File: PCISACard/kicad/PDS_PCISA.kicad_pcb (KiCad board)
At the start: 2 copper layers, 100 x 100 mm, 16 parts, among them J1 Bus_ISA_8bit, J2 Link 1, J3 Link 2, U1 74LS04, U2 74LS138, U3 8255, U4 74LS244, U5 74LS244, U6 74LS244

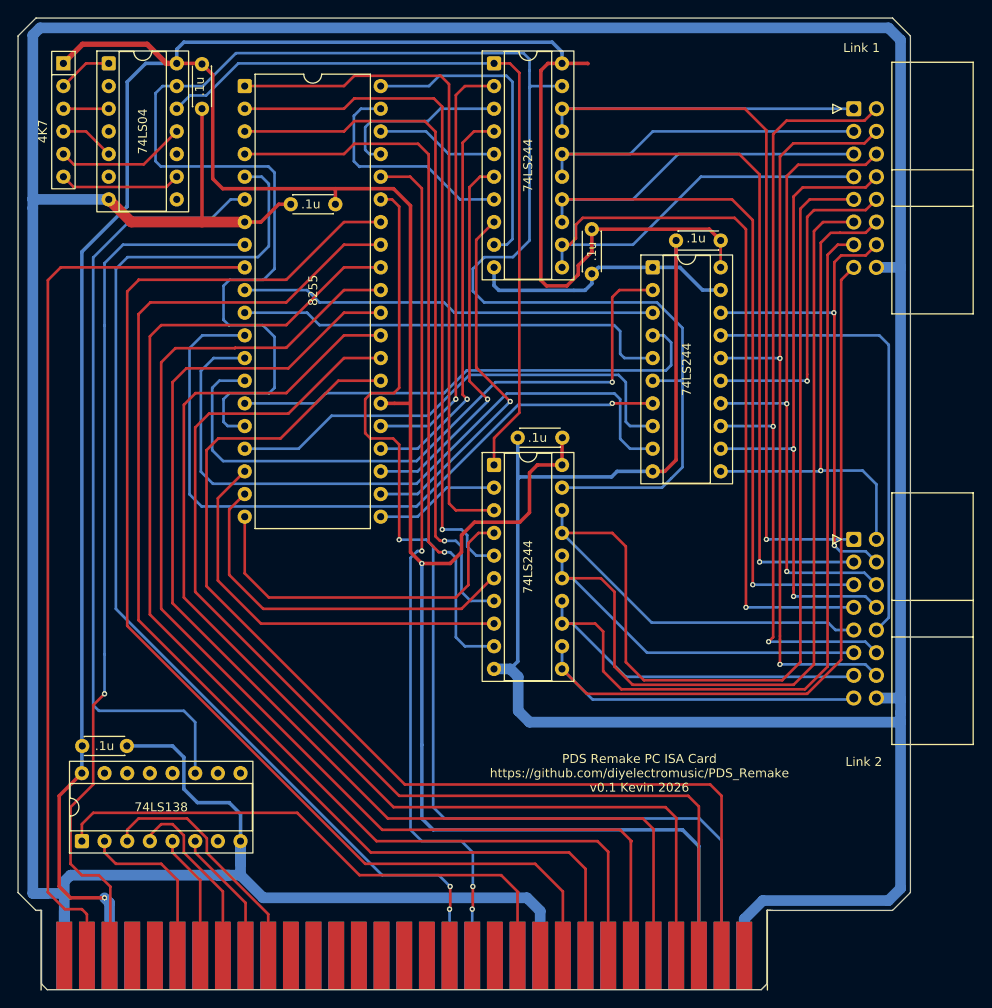
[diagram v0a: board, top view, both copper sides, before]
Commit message: Adjusting dimensions of PC card
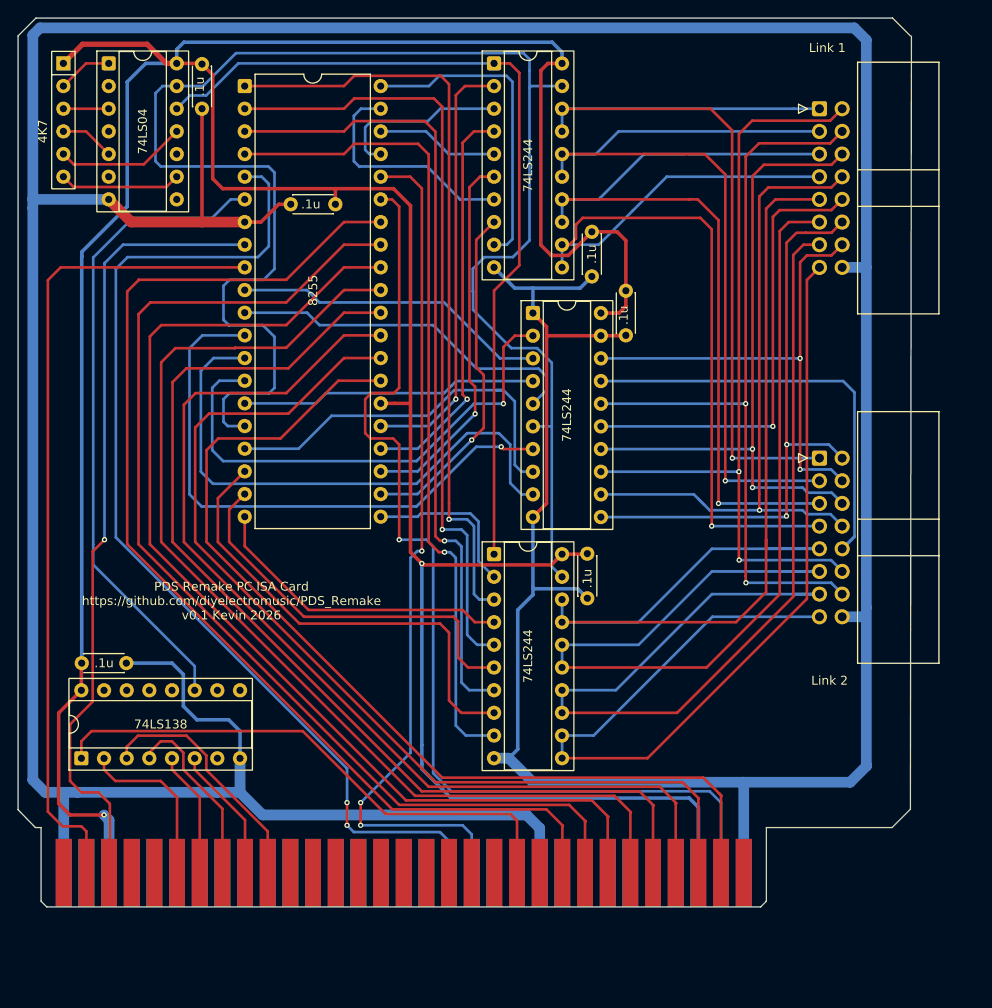
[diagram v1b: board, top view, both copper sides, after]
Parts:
- moved U6 14.4 mm to (107.7, 83.1)
- moved C4 13.3 mm to (113.8, 110.0), turned to -90 degrees
- moved C6 12.0 mm to (118.1, 80.6), turned to -90 degrees
- moved U4 10.0 mm to (103.3, 110.1)
- moved J3 9.88 mm to (139.8, 99.3)
- moved J1 9.28 mm to (131.3, 145.8)
- moved U2 9.28 mm to (57.1, 133.0)
- moved C2 9.28 mm to (57.1, 122.3)
- moved J2 3.84 mm to (139.8, 60.2)
- moved C5 0.29 mm to (114.3, 74.0)
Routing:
- net GND: track 621.4 -> 543.1 mm
- net VCC: track 417.0 -> 376.2 mm
- net Net-(J2-Pin_9): track 138.9 -> 115.5 mm
- net /PC1: track 54.5 -> 33.3 mm
- net /PC2: track 203.1 -> 184.5 mm
- net Net-(J2-Pin_11): track 131.1 -> 112.6 mm
- net /PC0: track 74.4 -> 56.9 mm
- net Net-(J2-Pin_3): track 113.4 -> 96.6 mm
- net Net-(J2-Pin_7): track 116.1 -> 99.3 mm
- net Net-(J2-Pin_5): track 111.8 -> 95.1 mm
- net Net-(J2-Pin_1): track 114.8 -> 98.0 mm
- net /PC5: track 80.4 -> 65.1 mm
- net /PC4: track 77.4 -> 62.3 mm
- net Net-(U2-O4): track 87.8 -> 72.9 mm
- net Net-(J2-Pin_10): track 36.7 -> 51.3 mm
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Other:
- board size 100 x 100 mm -> 100.1 x 90.7 mm

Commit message: PC Card Dimensions
More messing around with dimensions.  Probably closer to the original now, but still 100x100mm
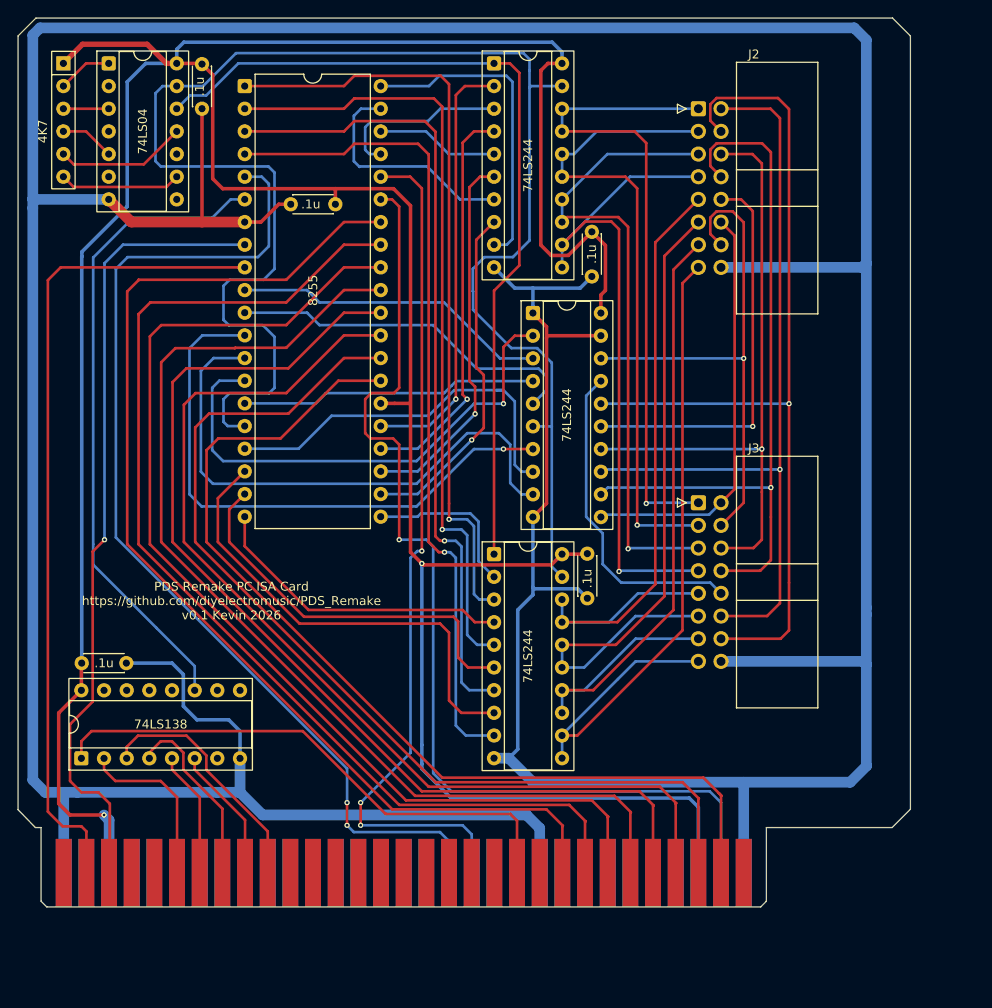
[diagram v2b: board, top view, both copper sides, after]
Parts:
- removed C6: .1u, Capacitor_THT:C_Disc_D4.3mm_W1.9mm_P5.00mm
- moved J3 14.5 mm to (126.2, 104.3)
- moved J2 13.6 mm to (126.2, 60.2)
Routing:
- net Net-(J2-Pin_9): track 115.5 -> 76.5 mm
- net Net-(J2-Pin_11): track 112.6 -> 77.5 mm
- net Net-(J2-Pin_13): track 112.2 -> 78.5 mm
- net Net-(J2-Pin_15): track 109.7 -> 81.1 mm
- net GND: track 543.1 -> 568.0 mm
- net Net-(J2-Pin_3): track 96.6 -> 72.4 mm
- net Net-(J2-Pin_1): track 98.0 -> 74.1 mm
- net Net-(J2-Pin_7): track 99.3 -> 76.1 mm
- net Net-(J2-Pin_5): track 95.1 -> 72.0 mm
- net Net-(J2-Pin_12): track 65.4 -> 46.8 mm, vias 2 -> 0
- net Net-(J2-Pin_4): track 87.3 -> 100.7 mm, vias 2 -> 1
- net Net-(J3-Pin_10): track 49.0 -> 36.6 mm
- net Net-(J2-Pin_8): track 74.8 -> 82.2 mm
- net Net-(J2-Pin_10): track 51.3 -> 45.2 mm
- net VCC: track 376.2 -> 371.5 mm
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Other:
- board size 100.1 x 90.7 mm -> 100 x 90.7 mm
